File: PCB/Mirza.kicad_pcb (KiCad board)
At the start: 2 copper layers, 79 x 34 mm, 105 parts, among them J1 In, J2 Out, J3 Power, Q1 BCM857BS, Q10 BCM857BS, Q11 BCM847BS, Q12 BCM847BS, Q13 2SC3324, Q14 2SA1312, Q15 2SA1312, Q16 2SA1312, Q17 2SC3324, Q18 2SC3324, Q19 BCM847BS, Q2 BCM847BS, Q20 BCM857BS, Q21 BCM857BS, Q22 BCM847BS, Q23 2SA1312, Q24 2SC3324, Q25 2SC3324, Q26 2SA1312, Q27 D45H11, Q28 D44H11, Q3 2SA1312, Q4 2SC3324, Q5 2SC3324, Q6 2SC3324, Q7 2SA1312, Q8 2SA1312, Q9 BCM857BS, U1 ADA4522-1

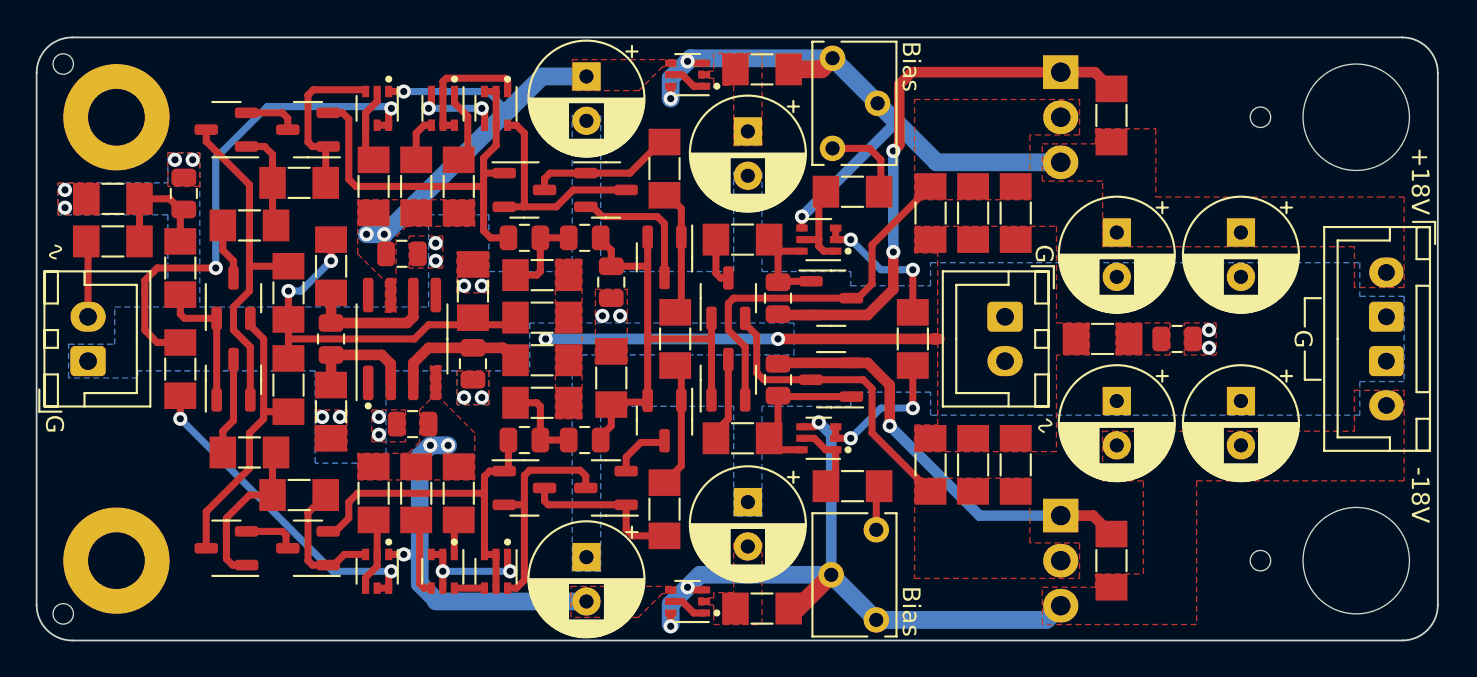
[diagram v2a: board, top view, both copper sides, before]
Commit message: 18/09/2023 update
Changed power header to JST XH 6-pin.
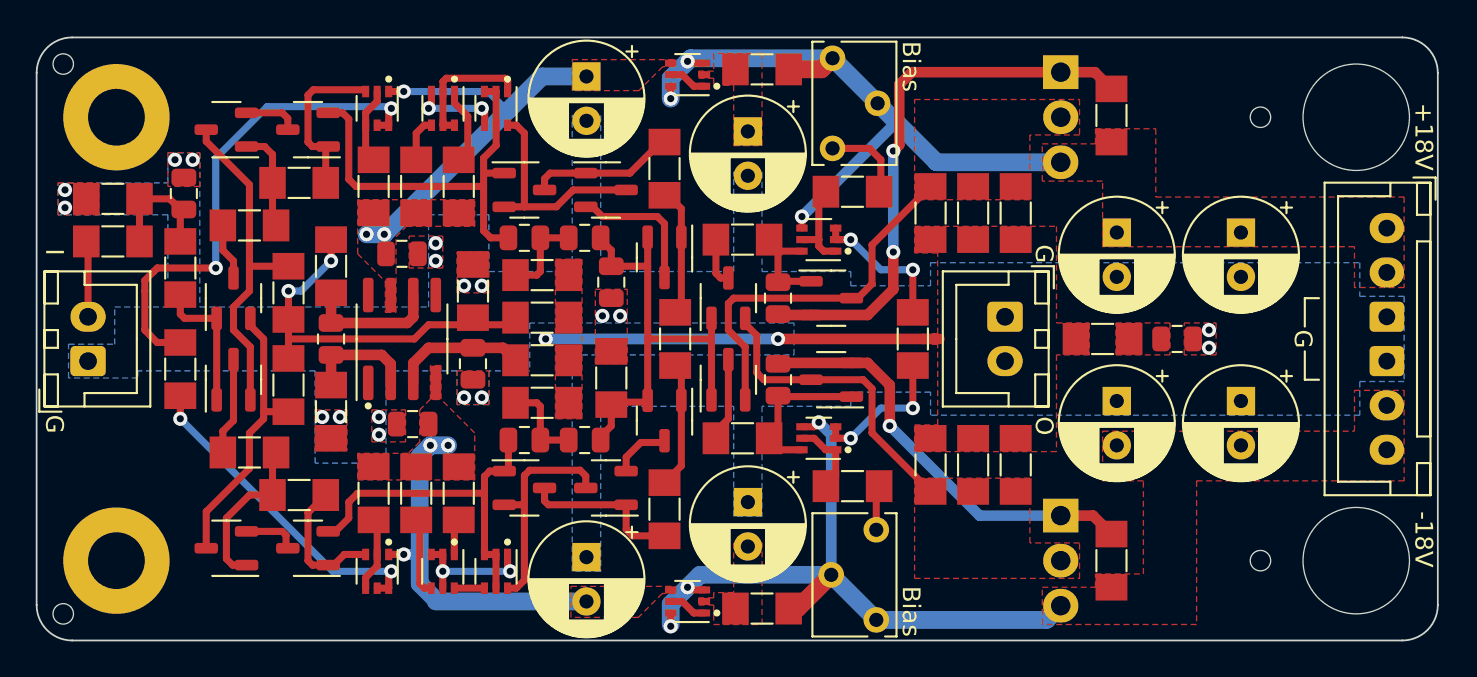
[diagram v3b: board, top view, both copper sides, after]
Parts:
- J3: footprint Ariamelon-Connector:JST_XH_B4B-XH-A_1x04_P2.50mm_Vertical_MiddleGND -> Ariamelon-Connector:JST_XH_B6B-XH-A_1x06_P2.50mm_Vertical_MiddleGND
- moved J3 2.50 mm to (136.6, 61.2)
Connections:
- J3 pad 2: GND -> +18V
- J3 pad 4: -18V -> GND
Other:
- board text added: "I"
- board text added: "O"
- board text removed: "∿"
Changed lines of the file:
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@@
   (title_block
     (title "Mirza Current-Feedback Amplifier Module")
-    (date "2023-09-17")
+    (date "2023-09-18")
     (rev "V1.0")
     (company "Created by Ariamelon (https://github.com/Ariamelon/Mirza/)")
@@
     )
   )
-  (footprint "Ariamelon-Connector:JST_XH_B4B-XH-A_1x04_P2.50mm_Vertical_MiddleGND" (layer "F.Cu")
-    (at 136.6 63.75 -90)
-    (descr "JST XH series connector, B4B-XH-A (http://www.jst-mfg.com/product/pdf/eng/eXH.pdf), generated with kicad-footprint-generator")
+  (footprint "Ariamelon-Connector:JST_XH_B6B-XH-A_1x06_P2.50mm_Vertical_MiddleGND" (layer "F.Cu")
+    (at 136.625 61.25 -90)
+    (descr "JST XH series connector, B6B-XH-A (http://www.jst-mfg.com/product/pdf/eng/eXH.pdf), generated with kicad-footprint-generator")
     (tags "connector JST XH vertical")
-    (property "LCSC" "")
     (property "Sheetfile" "Mirza.kicad_sch")
     (property "Sheetname" "")
-    (property "Voltage" "")
-    (property "exclude_from_bom" "")
-    (property "ki_description" "Generic connector, single row, 01x04, script generated (kicad-library-utils/schlib/autogen/connector/)")
+    (property "ki_description" "Generic connector, single row, 01x06, script generated (kicad-library-utils/schlib/autogen/connector/)")
     (property "ki_keywords" "connector")
-    (attr through_hole exclude_from_bom)
-    (fp_text reference "J3" (at 3.75 -3.55 90) (layer "F.SilkS") hide
+    (attr through_hole)
+    (fp_text reference "J3" (at 6.25 -3.55 90) (layer "F.SilkS") hide
         (effects (font (size 1 1) (thickness 0.15)))
     )
-    (fp_text value "Power" (at 3.75 5.1 90) (layer "F.Fab") hide
+    (fp_text value "Power" (at 6.25 4.6 90) (layer "F.Fab") hide
         (effects (font (size 1 1) (thickness 0.15)))
     )
-    (fp_text user "${REFERENCE}" (at 3.75 2.7 90) (layer "F.Fab")
+    (fp_text user "${REFERENCE}" (at 6.25 2.7 90) (layer "F.Fab")
         (effects (font (size 1 1) (thickness 0.15)))
     )
@@
     (fp_line (start -2.56 -2.46) (end -2.56 3.51)
       (stroke (width 0.12) (type solid)) (layer "F.SilkS"))
-    (fp_line (start -2.56 3.51) (end 10.06 3.51)
+    (fp_line (start -2.56 3.51) (end 15.06 3.51)
       (stroke (width 0.12) (type solid)) (layer "F.SilkS"))
     (fp_line (start -2.55 -2.45) (end -2.55 -1.7)
@@
     (fp_line (start -1.8 -0.2) (end -1.8 2.75)
       (stroke (width 0.12) (type solid)) (layer "F.SilkS"))
-    (fp_line (start -1.8 2.75) (end 3.75 2.75)
+    (fp_line (start -1.8 2.75) (end 6.25 2.75)
       (stroke (width 0.12) (type solid)) (layer "F.SilkS"))
     (fp_line (start -1.6 -2.75) (end -2.85 -2.75)
@@
     (fp_line (start 0.75 -2.45) (end 0.75 -1.7)
       (stroke (width 0.12) (type solid)) (layer "F.SilkS"))
-    (fp_line (start 0.75 -1.7) (end 6.75 -1.7)
+    (fp_line (start 0.75 -1.7) (end 11.75 -1.7)
       (stroke (width 0.12) (type solid)) (layer "F.SilkS"))
-    (fp_line (start 6.75 -2.45) (end 0.75 -2.45)
+    (fp_line (start 11.75 -2.45) (end 0.75 -2.45)
       (stroke (width 0.12) (type solid)) (layer "F.SilkS"))
-    (fp_line (start 6.75 -1.7) (end 6.75 -2.45)
+    (fp_line (start 11.75 -1.7) (end 11.75 -2.45)
       (stroke (width 0.12) (type solid)) (layer "F.SilkS"))
-    (fp_line (start 8.25 -2.45) (end 8.25 -1.7)
+    (fp_line (start 13.25 -2.45) (end 13.25 -1.7)
       (stroke (width 0.12) (type solid)) (layer "F.SilkS"))
-    (fp_line (start 8.25 -1.7) (end 10.05 -1.7)
+    (fp_line (start 13.25 -1.7) (end 15.05 -1.7)
       (stroke (width 0.12) (type solid)) (layer "F.SilkS"))
-    (fp_line (start 9.3 -0.2) (end 9.3 2.75)
+    (fp_line (start 14.3 -0.2) (end 14.3 2.75)
       (stroke (width 0.12) (type solid)) (layer "F.SilkS"))
-    (fp_line (start 9.3 2.75) (end 3.75 2.75)
+    (fp_line (start 14.3 2.75) (end 6.25 2.75)
       (stroke (width 0.12) (type solid)) (layer "F.SilkS"))
-    (fp_line (start 10.05 -2.45) (end 8.25 -2.45)
+    (fp_line (start 15.05 -2.45) (end 13.25 -2.45)
       (stroke (width 0.12) (type solid)) (layer "F.SilkS"))
-    (fp_line (start 10.05 -1.7) (end 10.05 -2.45)
+    (fp_line (start 15.05 -1.7) (end 15.05 -2.45)
       (stroke (width 0.12) (type solid)) (layer "F.SilkS"))
-    (fp_line (start 10.05 -0.2) (end 9.3 -0.2)
+    (fp_line (start 15.05 -0.2) (end 14.3 -0.2)
       (stroke (width 0.12) (type solid)) (layer "F.SilkS"))
-    (fp_line (start 10.06 -2.46) (end -2.56 -2.46)
+    (fp_line (start 15.06 -2.46) (end -2.56 -2.46)
       (stroke (width 0.12) (type solid)) (layer "F.SilkS"))
-    (fp_line (start 10.06 3.51) (end 10.06 -2.46)
+    (fp_line (start 15.06 3.51) (end 15.06 -2.46)
       (stroke (width 0.12) (type solid)) (layer "F.SilkS"))
     (fp_line (start -2.95 -2.85) (end -2.95 3.9)
       (stroke (width 0.05) (type solid)) (layer "F.CrtYd"))
-    (fp_line (start -2.95 3.9) (end 10.45 3.9)
+    (fp_line (start -2.95 3.9) (end 15.45 3.9)
       (stroke (width 0.05) (type solid)) (layer "F.CrtYd"))
-    (fp_line (start 10.45 -2.85) (end -2.95 -2.85)
+    (fp_line (start 15.45 -2.85) (end -2.95 -2.85)
       (stroke (width 0.05) (type solid)) (layer "F.CrtYd"))
-    (fp_line (start 10.45 3.9) (end 10.45 -2.85)
+    (fp_line (start 15.45 3.9) (end 15.45 -2.85)
       (stroke (width 0.05) (type solid)) (layer "F.CrtYd"))
     (fp_line (start -2.45 -2.35) (end -2.45 3.4)
       (stroke (width 0.1) (type solid)) (layer "F.Fab"))
-    (fp_line (start -2.45 3.4) (end 9.95 3.4)
+    (fp_line (start -2.45 3.4) (end 14.95 3.4)
       (stroke (width 0.1) (type solid)) (layer "F.Fab"))
     (fp_line (start -0.625 -2.35) (end 0 -1.35)
@@
     (fp_line (start 0 -1.35) (end 0.625 -2.35)
       (stroke (width 0.1) (type solid)) (layer "F.Fab"))
-    (fp_line (start 9.95 -2.35) (end -2.45 -2.35)
+    (fp_line (start 14.95 -2.35) (end -2.45 -2.35)
       (stroke (width 0.1) (type solid)) (layer "F.Fab"))
-    (fp_line (start 9.95 3.4) (end 9.95 -2.35)
+    (fp_line (start 14.95 3.4) (end 14.95 -2.35)
       (stroke (width 0.1) (type solid)) (layer "F.Fab"))
     (pad "1" thru_hole oval (at 0 0 270) (size 1.7 1.95) (drill 0.95) (layers "*.Cu" "*.Mask")
       (net 48 "+18V") (pinfunction "Pin_1") (pintype "passive"))
-    (pad "2" thru_hole roundrect (at 2.5 0 270) (size 1.7 1.95) (drill 0.95) (layers "*.Cu" "*.Mask") (roundrect_rratio 0.1470588235)
-      (net 1 "GND") (pinfunction "Pin_2") (pintype "passive"))
+    (pad "2" thru_hole oval (at 2.5 0 270) (size 1.7 1.95) (drill 0.95) (layers "*.Cu" "*.Mask")
+      (net 48 "+18V") (pinfunction "Pin_2") (pintype "passive"))
     (pad "3" thru_hole roundrect (at 5 0 270) (size 1.7 1.95) (drill 0.95) (layers "*.Cu" "*.Mask") (roundrect_rratio 0.1470588235)
       (net 1 "GND") (pinfunction "Pin_3") (pintype "passive"))
-    (pad "4" thru_hole oval (at 7.5 0 270) (size 1.7 1.95) (drill 0.95) (layers "*.Cu" "*.Mask")
-      (net 47 "-18V") (pinfunction "Pin_4") (pintype "passive"))
-    (model "${KICAD6_3DMODEL_DIR}/Connector_JST.3dshapes/JST_XH_B4B-XH-A_1x04_P2.50mm_Vertical.wrl"
+    (pad "4" thru_hole roundrect (at 7.5 0 270) (size 1.7 1.95) (drill 0.95) (layers "*.Cu" "*.Mask") (roundrect_rratio 0.1470588235)
+      (net 1 "GND") (pinfunction "Pin_4") (pintype "passive"))
+    (pad "5" thru_hole oval (at 10 0 270) (size 1.7 1.95) (drill 0.95) (layers "*.Cu" "*.Mask")
+      (net 47 "-18V") (pinfunction "Pin_5") (pintype "passive"))
+    (pad "6" thru_hole oval (at 12.5 0 270) (size 1.7 1.95) (drill 0.95) (layers "*.Cu" "*.Mask")
+      (net 47 "-18V") (pinfunction "Pin_6") (pintype "passive"))
+    (model "${KICAD6_3DMODEL_DIR}/Connector_JST.3dshapes/JST_XH_B6B-XH-A_1x06_P2.50mm_Vertical.wrl"
       (offset (xyz 0 0 0))
       (scale (xyz 1 1 1))
@@
   (gr_line (start 132 65.2) (end 132 66.8)
     (stroke (width 0.12) (type default)) (layer "F.SilkS"))
-  (gr_line (start 132 65.2) (end 132.9 65.2)
+  (gr_line (start 132 65.2) (end 132.8 65.2)
     (stroke (width 0.12) (type default)) (layer "F.SilkS"))
   (gr_line (start 132 68.2) (end 132 69.8)
     (stroke (width 0.12) (type default)) (layer "F.SilkS"))
-  (gr_line (start 132 69.8) (end 132.9 69.8)
+  (gr_line (start 132 69.8) (end 132.8 69.8)
     (stroke (width 0.12) (type default)) (layer "F.SilkS"))
   (gr_line (start 95.8 74.4) (end 95.8 75.1)
@@
     (effects (font (size 1 1) (thickness 0.15)) (justify mirror))
   )
-  (gr_text "∿" (at 117.4 72.4 255) (layer "F.SilkS")
+  (gr_text "O" (at 117.3 72.4 270) (layer "F.SilkS")
     (effects (font (size 1 1) (thickness 0.15)))
   )
@@
     (effects (font (size 1 1) (thickness 0.15)))
   )
-  (gr_text "-18V" (at 138.5 76.3 270) (layer "F.SilkS")
+  (gr_text "-18V" (at 138.7 78.8 -90) (layer "F.SilkS")
     (effects (font (size 1 1) (thickness 0.15)))
   )
-  (gr_text "+18V" (at 138.5 58.6 -90) (layer "F.SilkS")
+  (gr_text "+18V" (at 138.7 56.1 270) (layer "F.SilkS")
     (effects (font (size 1 1) (thickness 0.15)))
   )
-  (gr_text "∿" (at 61.6 62.6 -90) (layer "F.SilkS")
+  (gr_text "I" (at 61.5 62.6 270) (layer "F.SilkS")
     (effects (font (size 1 1) (thickness 0.15)))
   )

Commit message: 20/09/2023 update
Shortened board by removing one pair of capacitors and increasing the size of the other and reducing the number of emitter resistors.
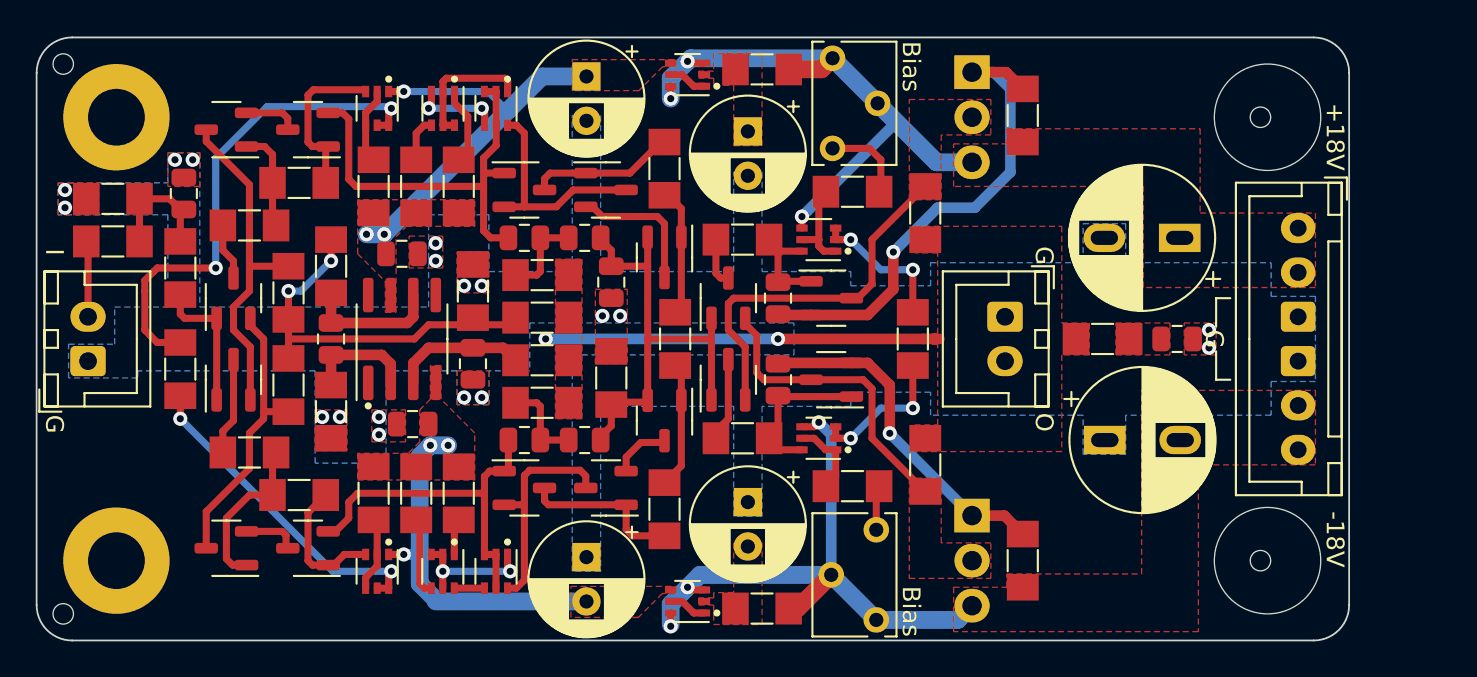
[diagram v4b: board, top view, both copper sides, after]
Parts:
- removed the C18 at (128.4, 61.5)
- removed the C19 at (128.4, 71.0)
- removed R32, R33, R34, R35: 1R5, Resistor_SMD:R_MiniMELF_MMA-0204
- C16, C17: value 100u -> 470u; footprint Ariamelon-Device:CP_Radial_D6.3mm_P2.50mm -> Ariamelon-Device:CP_Radial_D8.0mm_P3.50mm_P5.00mm
- R36, R37: value 1R5 -> 0R47
- moved J3 5.00 mm to (131.6, 61.2)
- moved Q27 5.00 mm to (113.2, 55.0)
- moved Q28 5.00 mm to (113.2, 80.0)
- moved R30 5.00 mm to (116.1, 54.9)
- moved R31 5.00 mm to (116.1, 80.0)
- moved C16 3.94 mm to (125.3, 61.8), turned to 180 degrees
- moved C17 2.44 mm to (120.3, 73.2), turned to 0 degrees
- moved R36 0.30 mm to (110.6, 60.4)
- moved R37 0.30 mm to (110.6, 74.6)
- renumbered C20 to C18, C21 to C19
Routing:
- net -18V: track 40.0 -> 35.0 mm
- net +18V: track 38.6 -> 33.6 mm
- net Net-(Q26-C): track 24.2 -> 19.4 mm
- net Net-(Q25-C): track 31.4 -> 28.2 mm, vias 2 -> 1
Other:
- board size 79 x 34 mm -> 74 x 34 mm

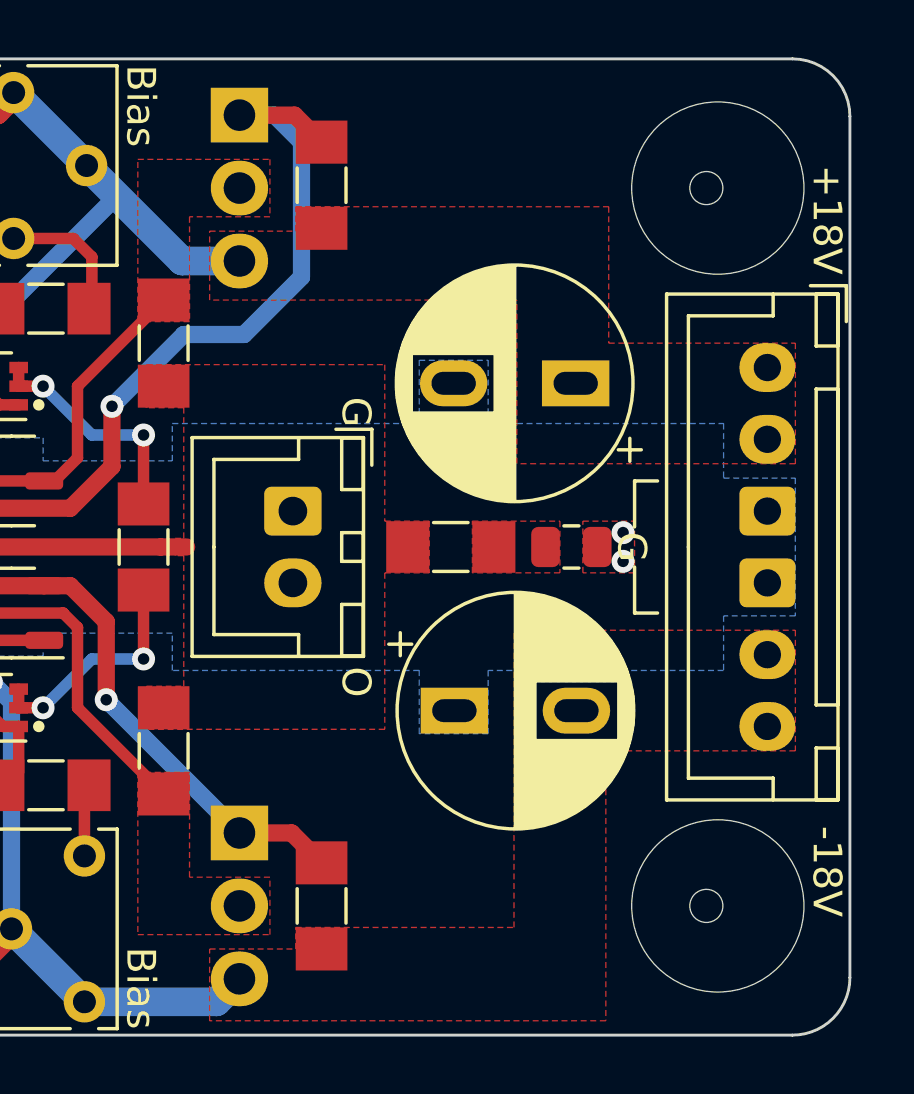
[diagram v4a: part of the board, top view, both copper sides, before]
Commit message: 22/03/2023 update
Changed power connector to phoenix terminal block.
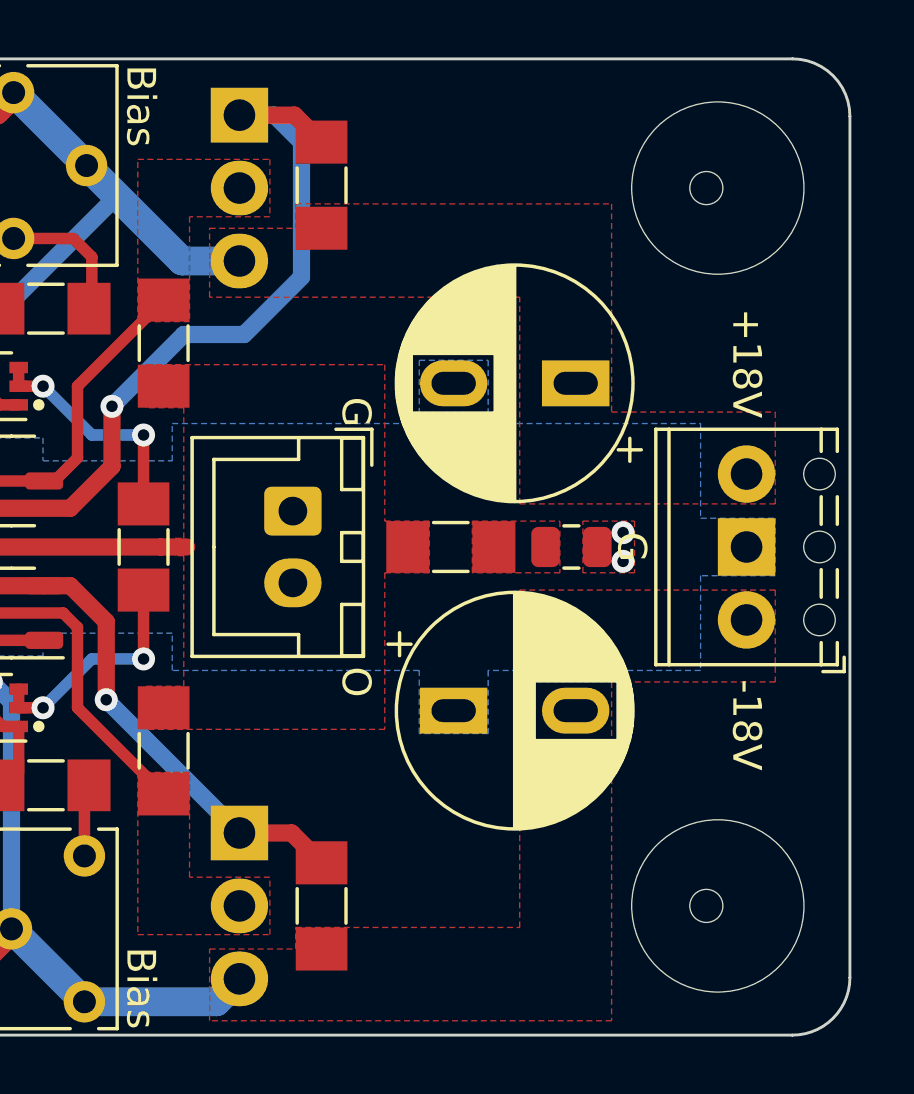
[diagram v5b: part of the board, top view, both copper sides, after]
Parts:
- J3: footprint Ariamelon-Connector:JST_XH_B6B-XH-A_1x06_P2.50mm_Vertical_MiddleGND -> Ariamelon-Connector:TerminalBlock_Phoenix_MPT-0,5-3-2.54_1x03_P2.54mm_Horizontal_MiddleGND
- moved J3 8.82 mm to (130.9, 70.0), turned to 90 degrees
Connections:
- J3 pad 1: +18V -> -18V
- J3 pad 2: +18V -> GND
- J3 pad 3: GND -> +18V
